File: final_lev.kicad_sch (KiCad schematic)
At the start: 0 parts

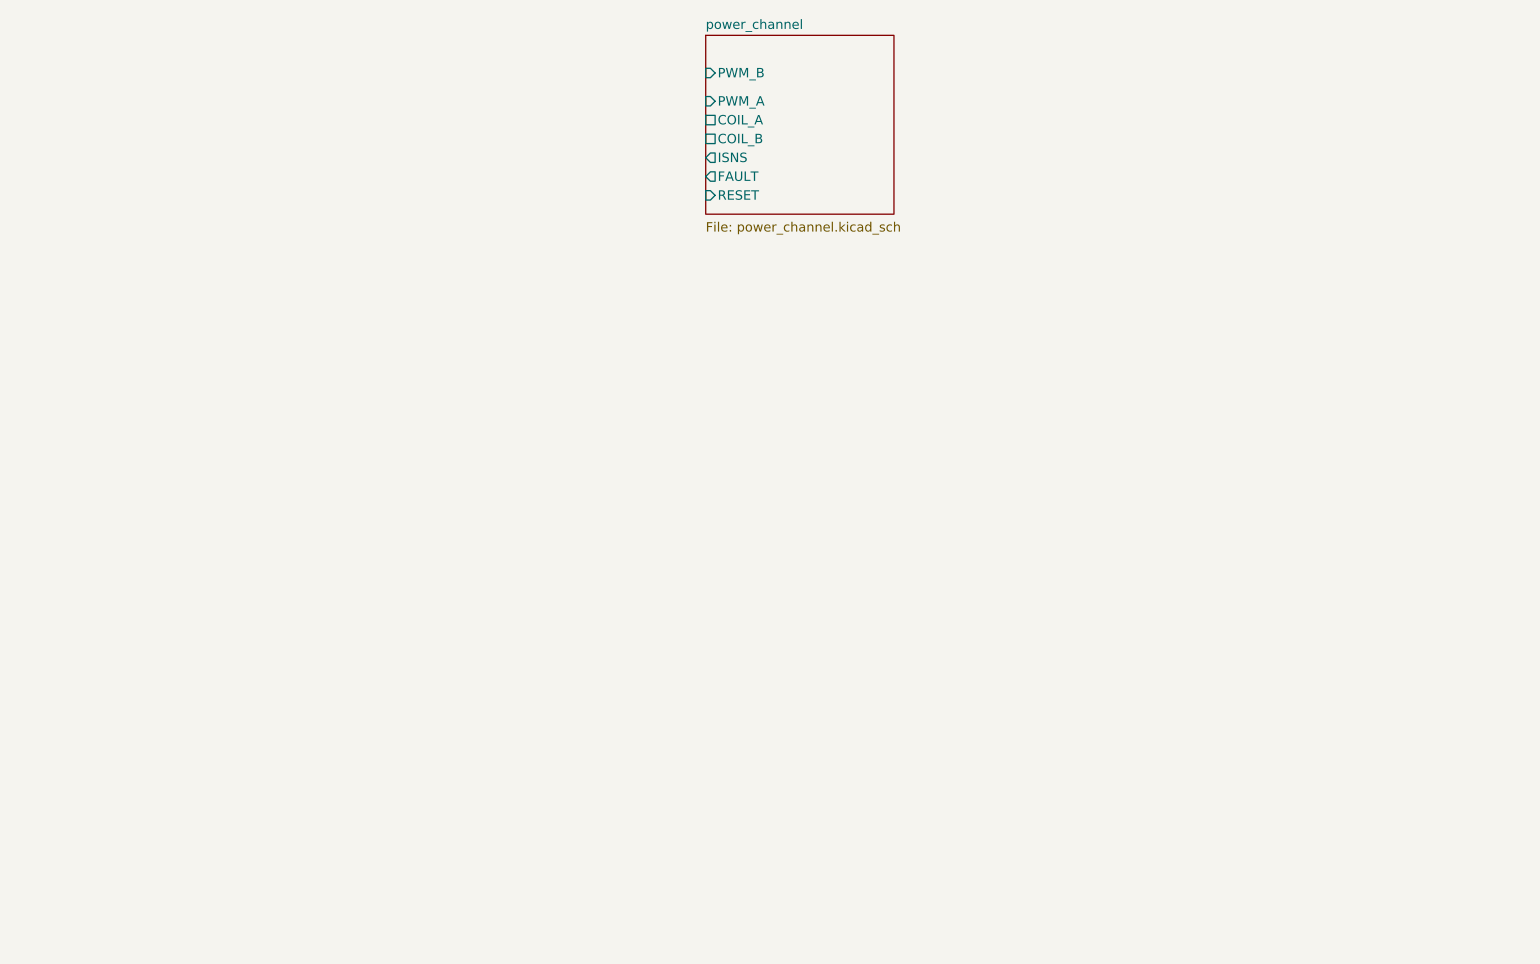
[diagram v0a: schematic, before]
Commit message: Schematic complete: BUS, IO_PROTECT, dual power_channel instances, ERC clean
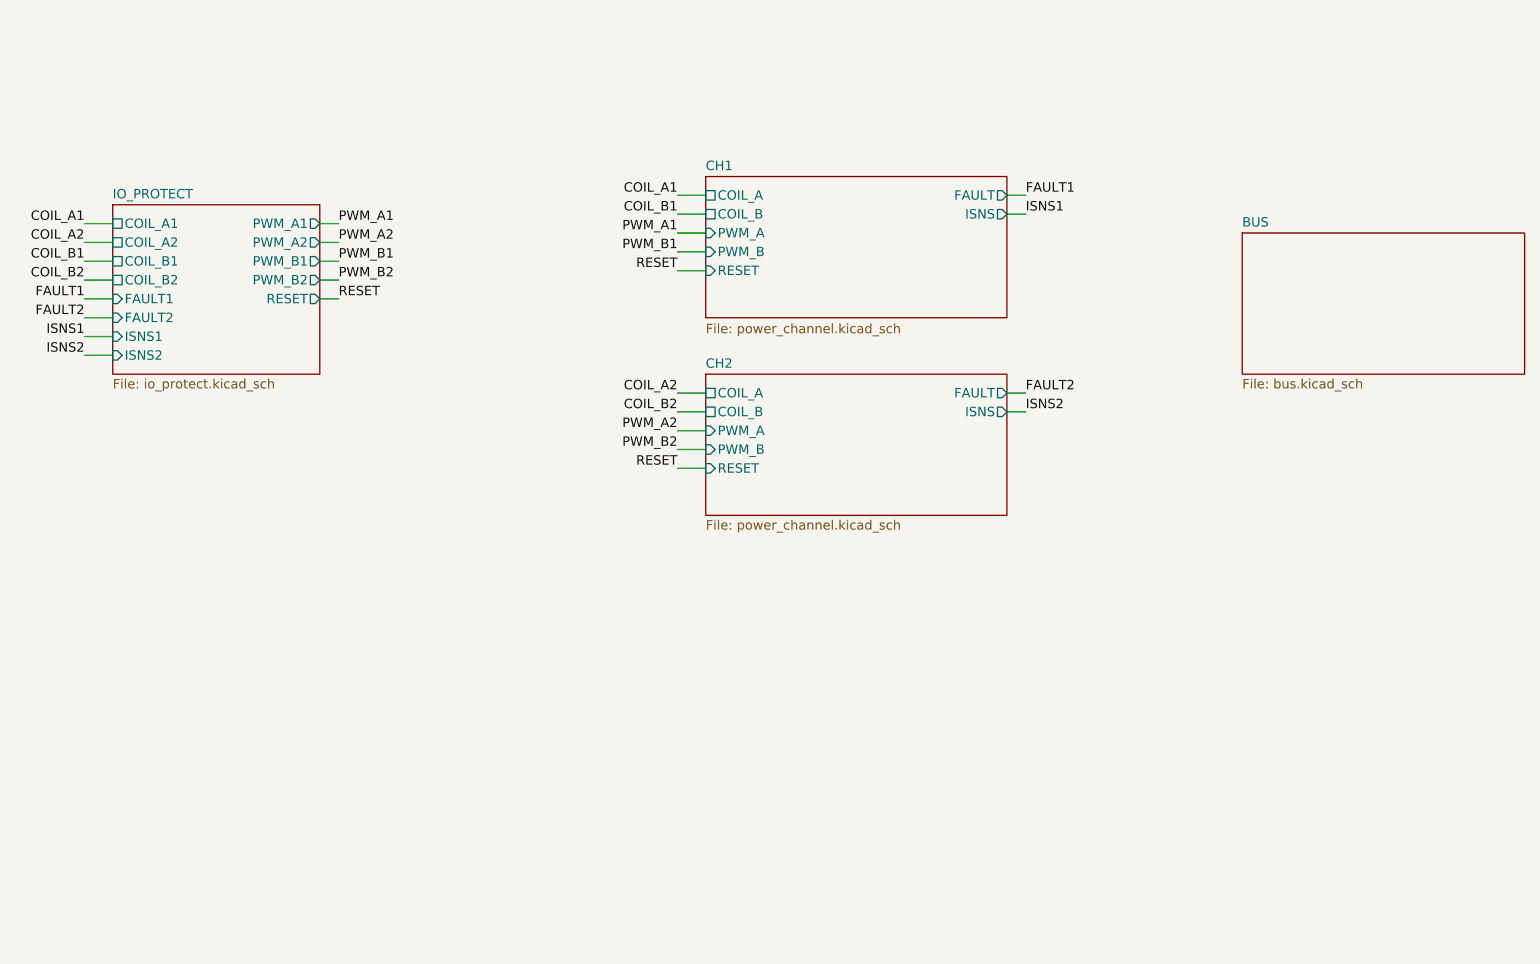
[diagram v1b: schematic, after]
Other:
- sheet power_channel renamed CH1
- added sheet BUS (bus.kicad_sch)
- added sheet CH2 (power_channel.kicad_sch)
- added sheet IO_PROTECT (io_protect.kicad_sch)

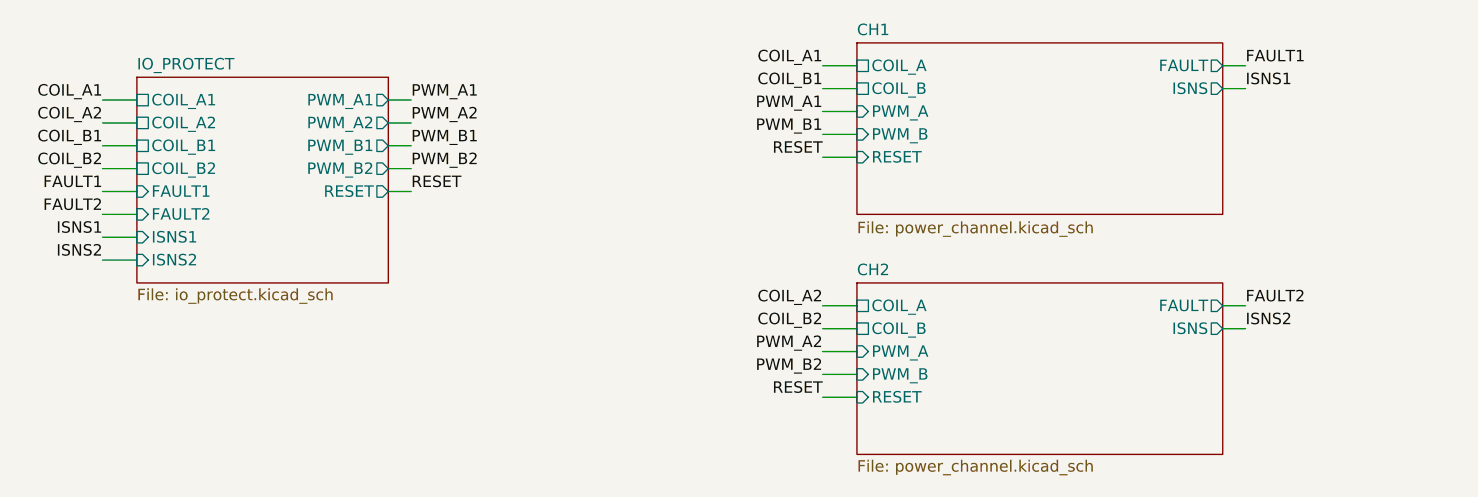
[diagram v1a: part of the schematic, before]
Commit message: Adversarial review fixes: set-dominant latch, MCU enable, 3V3 hold-up, sense chain, 16-way connector
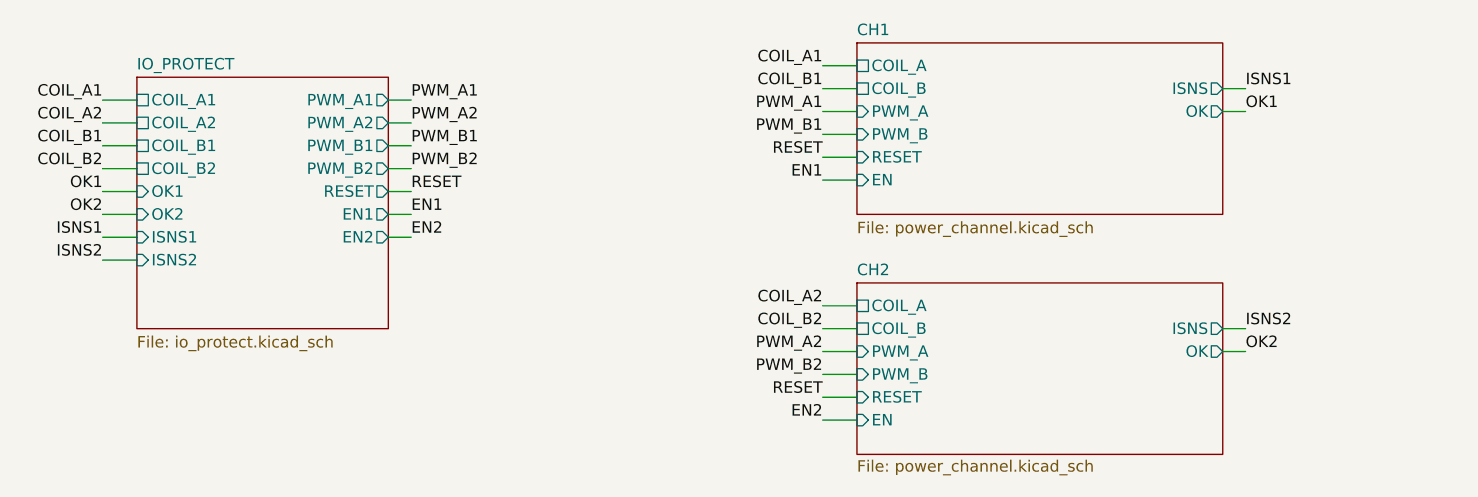
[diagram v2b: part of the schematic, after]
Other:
- sheet CH1 ports: added EN, OK; removed FAULT
- sheet CH2 ports: added EN, OK; removed FAULT
- sheet IO_PROTECT ports: added EN1, EN2, OK1, OK2; removed FAULT1, FAULT2
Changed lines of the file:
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@@
-	(wire
-		(pts
-			(xy 170.18 146.05) (xy 172.72 146.05)
-		)
-		(stroke
-			(width 0)
-			(type default)
-		)
-	)
 	(wire
 		(pts
@@
 	(wire
 		(pts
-			(xy 170.18 119.38) (xy 172.72 119.38)
-		)
-		(stroke
-			(width 0)
-			(type default)
-		)
-	)
-	(wire
-		(pts
 			(xy 125.73 148.59) (xy 129.54 148.59)
 		)
@@
 	(wire
 		(pts
+			(xy 125.73 132.08) (xy 129.54 132.08)
+		)
+		(stroke
+			(width 0)
+			(type default)
+		)
+	)
+	(wire
+		(pts
 			(xy 125.73 146.05) (xy 129.54 146.05)
 		)
@@
 	(wire
 		(pts
+			(xy 170.18 151.13) (xy 172.72 151.13)
+		)
+		(stroke
+			(width 0)
+			(type default)
+		)
+	)
+	(wire
+		(pts
 			(xy 77.47 125.73) (xy 80.01 125.73)
 		)
@@
 	(wire
 		(pts
+			(xy 77.47 138.43) (xy 80.01 138.43)
+		)
+		(stroke
+			(width 0)
+			(type default)
+		)
+	)
+	(wire
+		(pts
 			(xy 125.73 151.13) (xy 129.54 151.13)
 		)
@@
 		)
 	)
-	(label "FAULT2"
-		(at 172.72 146.05 0)
+	(wire
+		(pts
+			(xy 170.18 124.46) (xy 172.72 124.46)
+		)
+		(stroke
+			(width 0)
+			(type default)
+		)
+	)
+	(wire
+		(pts
+			(xy 125.73 158.75) (xy 129.54 158.75)
+		)
+		(stroke
+			(width 0)
+			(type default)
+		)
+	)
+	(wire
+		(pts
+			(xy 77.47 135.89) (xy 80.01 135.89)
+		)
+		(stroke
+			(width 0)
+			(type default)
+		)
+	)
+	(label "OK2"
+		(at 172.72 151.13 0)
 		(effects
 			(font
@@
 		)
 	)
+	(label "EN2"
+		(at 125.73 158.75 180)
+		(effects
+			(font
+				(size 1.27 1.27)
+			)
+			(justify right bottom)
+		)
+	)
+	(label "EN2"
+		(at 80.01 138.43 0)
+		(effects
+			(font
+				(size 1.27 1.27)
+			)
+			(justify left bottom)
+		)
+	)
+	(label "EN1"
+		(at 80.01 135.89 0)
+		(effects
+			(font
+				(size 1.27 1.27)
+			)
+			(justify left bottom)
+		)
+	)
 	(label "PWM_B1"
 		(at 125.73 127 180)
@@
 		)
 	)
+	(label "EN1"
+		(at 125.73 132.08 180)
+		(effects
+			(font
+				(size 1.27 1.27)
+			)
+			(justify right bottom)
+		)
+	)
 	(label "PWM_B2"
 		(at 80.01 130.81 0)
@@
 		)
 	)
-	(label "FAULT2"
+	(label "OK2"
 		(at 45.72 135.89 180)
 		(effects
@@
 		)
 	)
-	(label "FAULT1"
+	(label "OK1"
 		(at 45.72 133.35 180)
 		(effects
@@
 		)
 	)
-	(label "FAULT1"
-		(at 172.72 119.38 0)
+	(label "OK1"
+		(at 172.72 124.46 0)
 		(effects
 			(font
@@
 	(sheet
 		(at 49.53 120.65)
-		(size 27.94 22.86)
+		(size 27.94 27.94)
 		(exclude_from_sim no)
 		(in_bom yes)
 		(on_board yes)
 		(dnp no)
-		(fields_autoplaced yes)
 		(stroke
 			(width 0.1524)
@@
 		)
 		(property "Sheetfile" "io_protect.kicad_sch"
-			(at 49.53 144.0946 0)
+			(at 49.53 149.352 0)
 			(show_name no)
 			(do_not_autoplace no)
@@
 			)
 		)
-		(pin "FAULT1" input
+		(pin "OK1" input
 			(at 49.53 133.35 180)
 			(effects
@@
 			)
 		)
-		(pin "FAULT2" input
+		(pin "OK2" input
 			(at 49.53 135.89 180)
 			(effects
@@
 		(pin "RESET" output
 			(at 77.47 133.35 0)
+			(effects
+				(font
+					(size 1.27 1.27)
+				)
+				(justify right)
+			)
+		)
+		(pin "EN1" output
+			(at 77.47 135.89 0)
+			(effects
+				(font
+					(size 1.27 1.27)
+				)
+				(justify right)
+			)
+		)
+		(pin "EN2" output
+			(at 77.47 138.43 0)
 			(effects
 				(font
@@
 			)
 		)
-		(pin "FAULT" output
-			(at 170.18 146.05 0)
-			(effects
-				(font
-					(size 1.27 1.27)
-				)
-				(justify right)
-			)
-		)
 		(pin "ISNS" output
 			(at 170.18 148.59 0)
+			(effects
+				(font
+					(size 1.27 1.27)
+				)
+				(justify right)
+			)
+		)
+		(pin "EN" input
+			(at 129.54 158.75 180)
+			(effects
+				(font
+					(size 1.27 1.27)
+				)
+				(justify left)
+			)
+		)
+		(pin "OK" output
+			(at 170.18 151.13 0)
 			(effects
 				(font
@@
 			)
 		)
-		(pin "FAULT" output
-			(at 170.18 119.38 0)
-			(effects
-				(font
-					(size 1.27 1.27)
-				)
-				(justify right)
-			)
-		)
 		(pin "ISNS" output
 			(at 170.18 121.92 0)
 			(effects
 				(font
+					(size 1.27 1.27)
+				)
+				(justify right)
+			)
+		)
+		(pin "EN" input
+			(at 129.54 132.08 180)
+			(effects
+				(font
+					(size 1.27 1.27)
+				)
+				(justify left)
+			)
+		)
+		(pin "OK" output
+			(at 170.18 124.46 0)
+			(effects
+				(font

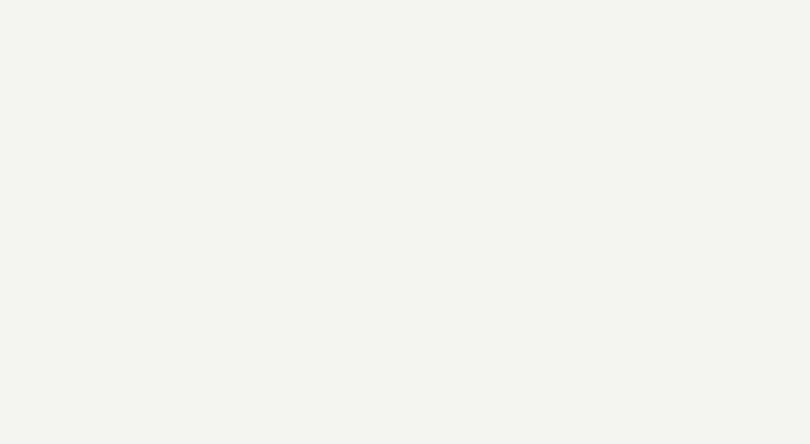
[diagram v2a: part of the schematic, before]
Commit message: PCB placement complete (160x140, 184 fp, 0 courtyard overlaps); layout phase docs + lay.py; handoff
- Board resized 160x100 -> 160x140 after the courtyard-vs-pad-extent error
- Full placement of all 184 footprints, DRC clean except unconnected
- J203 moved inside the outline (x 107.0 -> 107.5), 0.450 mm margin
- docs/20_layout_phase.md: floorplan, verified metrics, CH2 leg-swap analysis
- docs/00_design_log.md: layout-phase entry incl. retraction of the
  'commutation loops trade values' claim (they are unchanged)
- tools/lay.py: courtyard-accurate layout checker, rescued from /tmp
- HANDOFF.md: remaining steps 1-3 with exact coordinates, transfer options

CH2 leg A/B swap analysed and verified but NOT applied.
2-layer vs 4-layer still undecided.
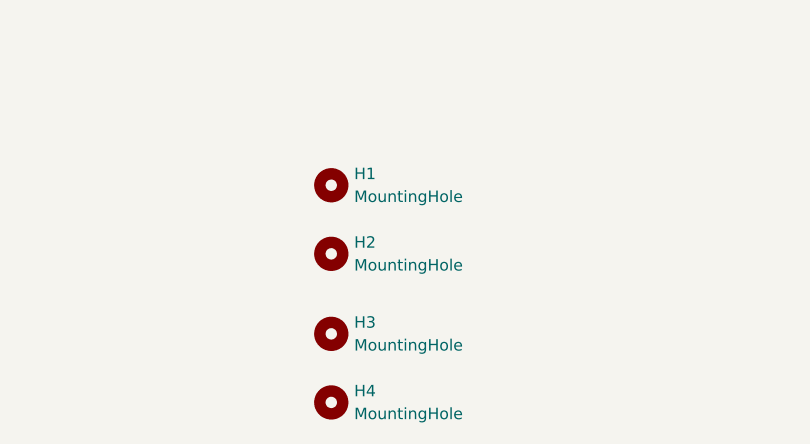
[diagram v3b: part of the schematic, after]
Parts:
- added H1, H2, H3, H4: MountingHole, MountingHole:MountingHole_3.2mm_M3_Pad, symbol Mechanical:MountingHole
